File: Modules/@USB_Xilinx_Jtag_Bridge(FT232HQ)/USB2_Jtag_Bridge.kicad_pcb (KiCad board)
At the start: 4 copper layers, 17.9 x 22.3 mm, 37 parts, among them J1 USB-C16PSMT01, J2 Conn_01x06_Male, U1 FT232H, U2 93LC56BxxOT, U3 mp9442, Y1 12M

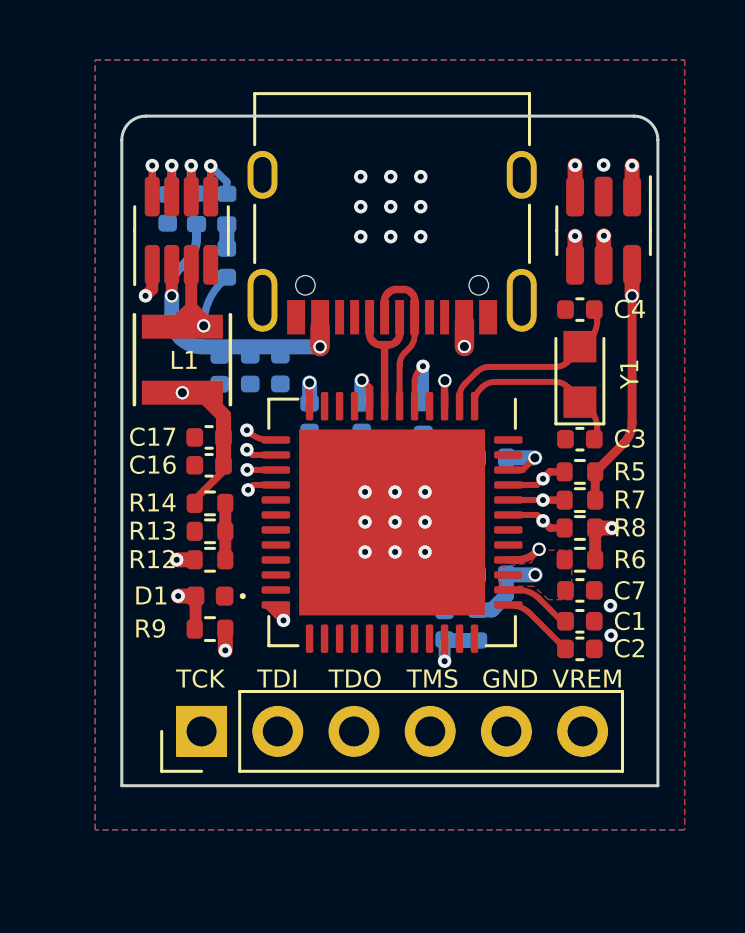
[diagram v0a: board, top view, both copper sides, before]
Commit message: Finish USB2_Jtag_Bridge
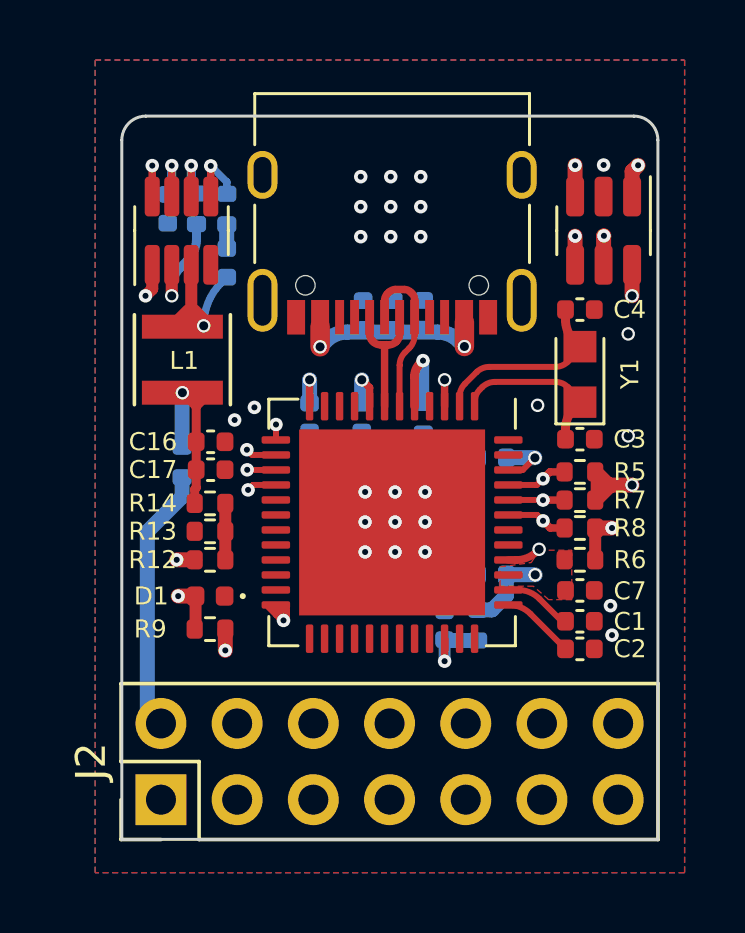
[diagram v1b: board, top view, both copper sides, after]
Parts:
- added Jumper1: Jumper, Resistor_SMD:R_0402_1005Metric, B.Cu at (135.0, 77.5)
- J2: footprint Connector_PinHeader_2.54mm:PinHeader_1x06_P2.54mm_Vertical -> Connector_PinHeader_2.54mm:PinHeader_2x07_P2.54mm_Vertical
- moved C11 7.04 mm to (143.0, 72.6), turned to 90 degrees
- moved C12 5.11 mm to (142.0, 72.6), turned to 90 degrees
- moved C13 3.30 mm to (141.0, 72.6), turned to 90 degrees
- moved J2 2.65 mm to (134.3, 88.8)
- moved C17 1.08 mm to (135.9, 77.8), turned to 0 degrees
- moved C16 0.79 mm to (135.9, 76.9), turned to 0 degrees
- turned C3 to 180 degrees
- turned C4 to 180 degrees
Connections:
- J2 pad 1: TCK -> unconnected-(J2-Pad1)
- J2 pad 2: TDI -> Net-(J2-Pad2)
- J2 pad 3: TDO -> VSS
- J2 pad 6: 3.3V -> TCK
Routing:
- net 3.3V: track 24.3 -> 7.26 mm
- net Net-(J2-Pad2): track 0.00 -> 8.87 mm
- net +3V3: track 52.9 -> 48.0 mm, vias 7 -> 8
- net TMS: track 11.5 -> 8.93 mm
- net VBUS: track 39.0 -> 37.0 mm
- net TDI: track 11.9 -> 13.5 mm
- net TCK: track 11.9 -> 11.2 mm
- net VSS: vias 21 -> 26
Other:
- board size 17.9 x 22.3 mm -> 17.9 x 24.1 mm
- board text removed: "GND"
- board text removed: "TCK"
- board text removed: "TDI"
- board text removed: "TDO"
- board text removed: "TMS"
- board text removed: "VREM"

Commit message: Crystal footprint fix
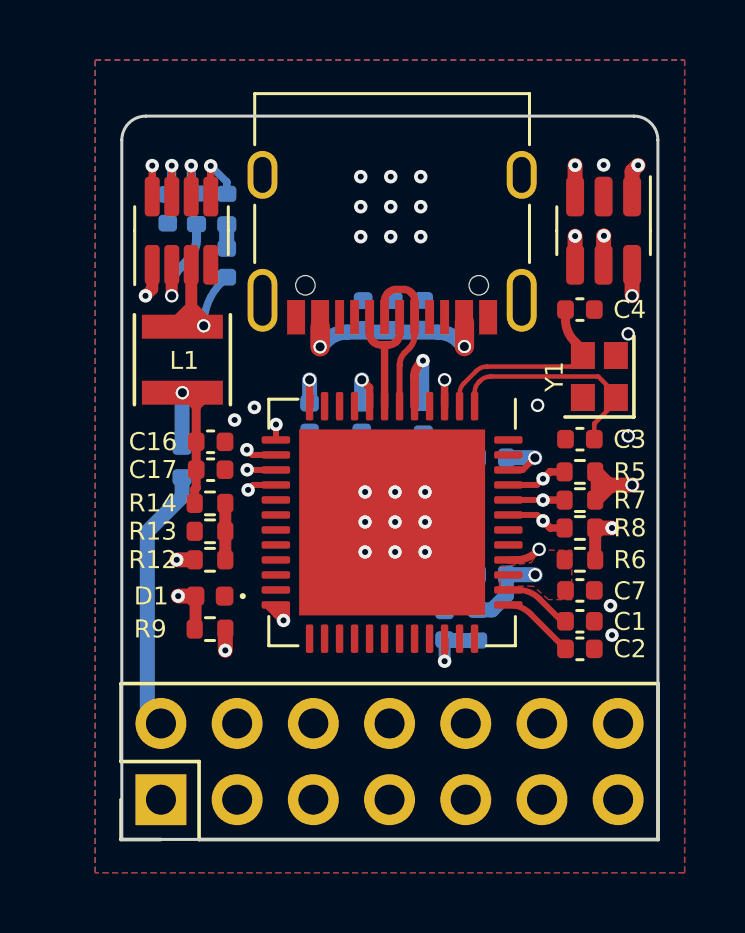
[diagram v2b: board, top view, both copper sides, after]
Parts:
- Y1: footprint Crystal:Crystal_SMD_TXC_9HT11-2Pin_2.0x1.2mm_HandSoldering -> Crystal:Crystal_SMD_2016-4Pin_2.0x1.6mm
- moved Y1 0.65 mm to (148.9, 74.7)
- turned C3 to 0 degrees
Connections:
- Y1 pad 2: Net-(C4-Pad2) -> VSS
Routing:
- net Net-(C3-Pad2): track 5.75 -> 7.50 mm
